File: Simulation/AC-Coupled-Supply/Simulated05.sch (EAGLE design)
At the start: 19 parts, among them IC1 78L05Z

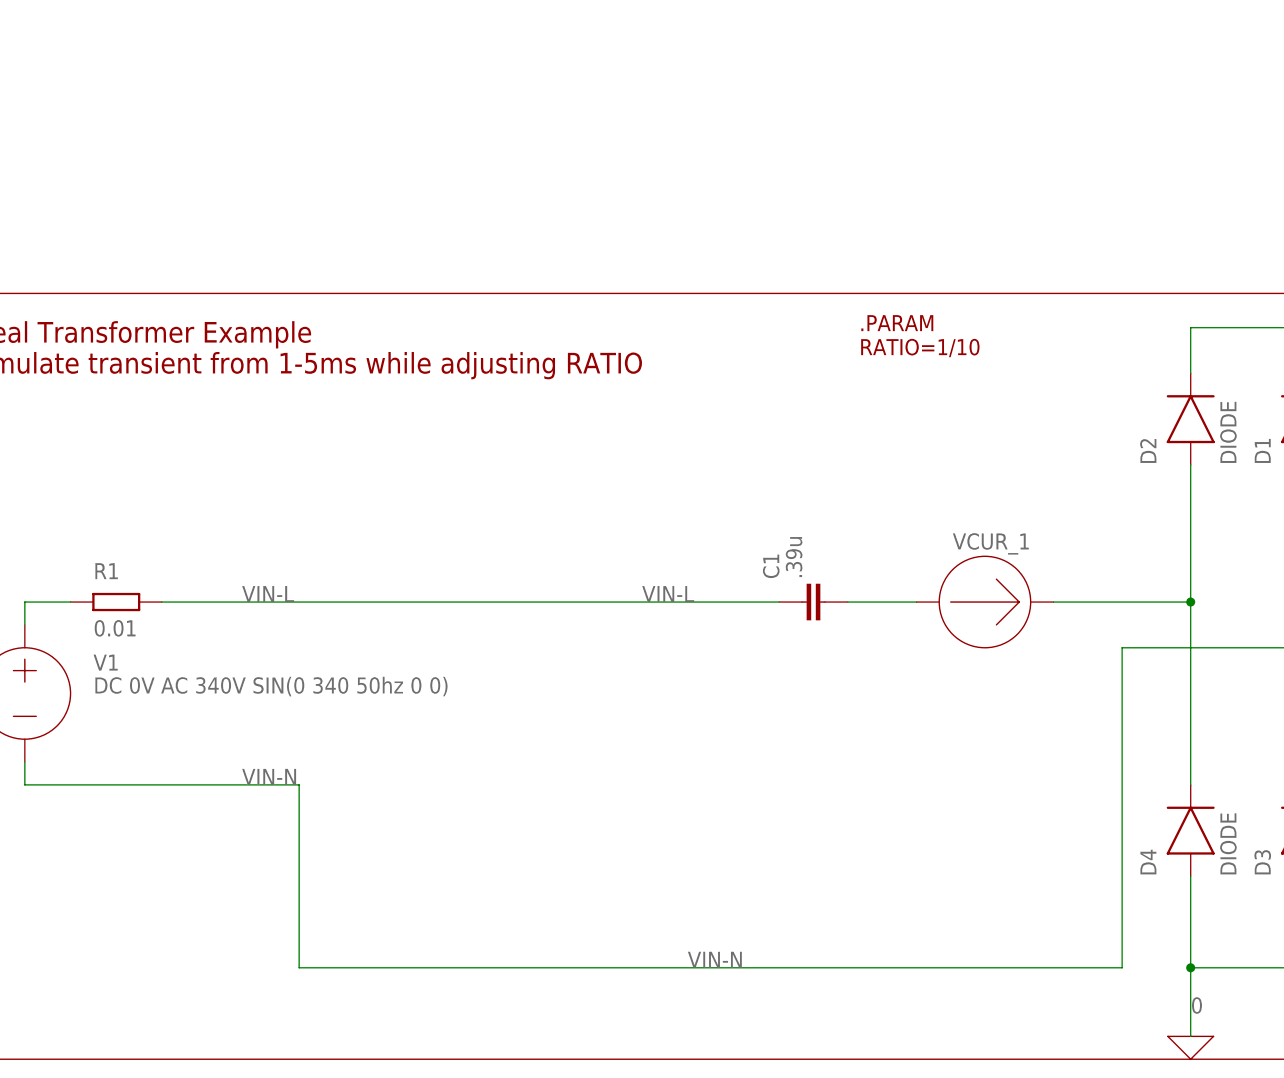
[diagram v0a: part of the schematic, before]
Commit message: measurement with differential probe
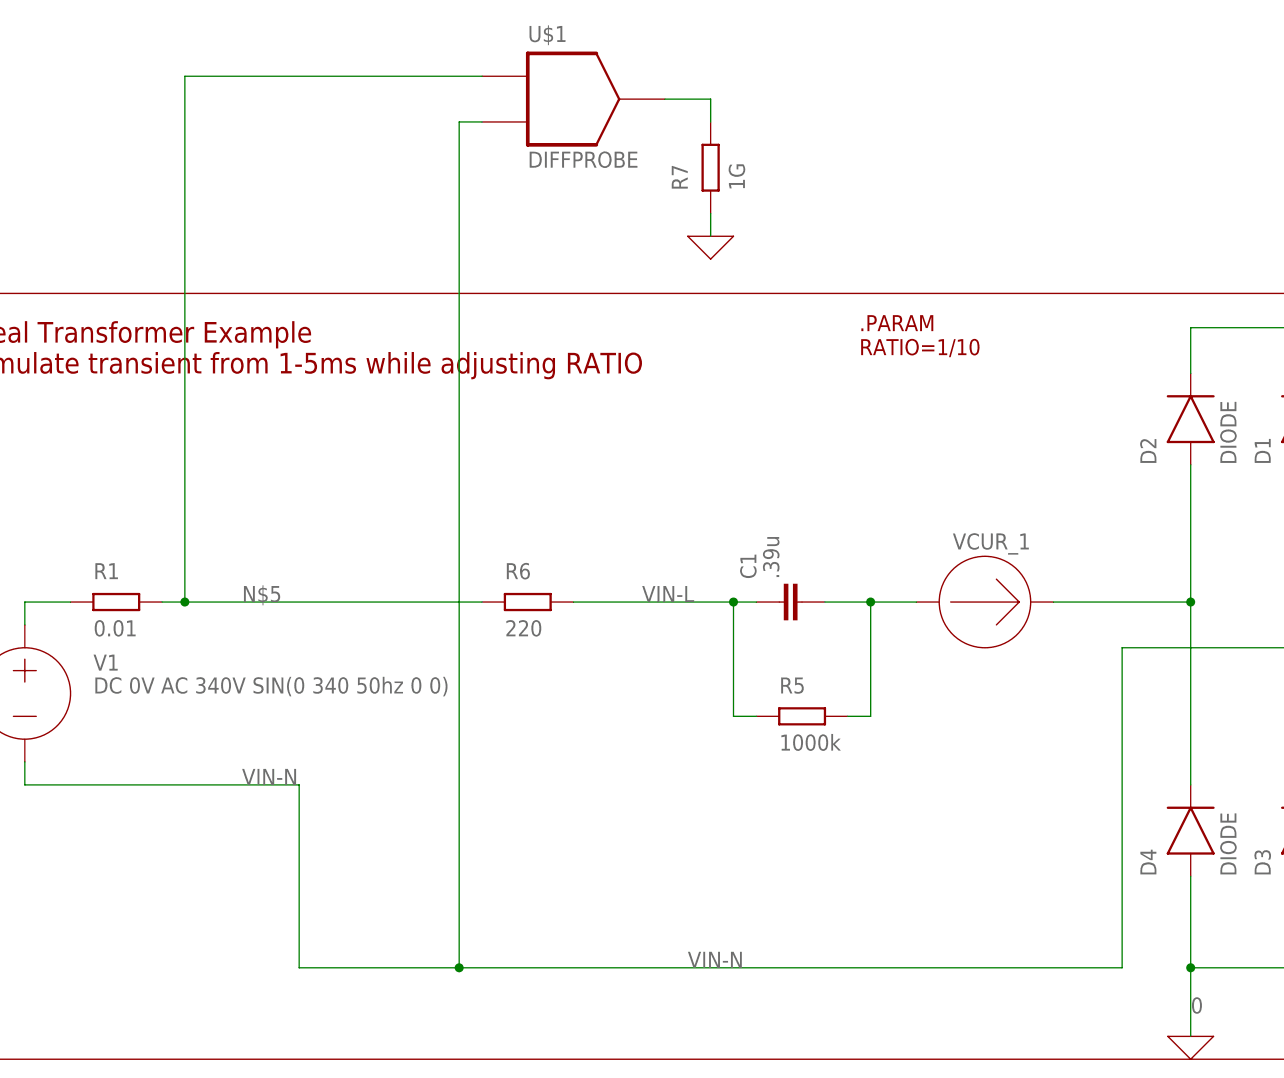
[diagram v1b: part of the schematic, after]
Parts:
- added R5: 1000k, ngspice-simulation:R
- added R6: 220, ngspice-simulation:R
- added R7: 1G, ngspice-simulation:R
- added U$1: DIFFPROBE, simulation:DIFFPROBE
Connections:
- new net DIFF: R7.2, U$1.OUT
- new net N$5: R1.2, R6.1, U$1.IN+
- net 0: now also R7.1
- net N$4: now also R5.2
- net VIN-L: now also R5.1, R6.2; no longer R1.2
- net VIN-N: now also U$1.IN-
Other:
- moved on the sheet: C1
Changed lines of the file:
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@@
 <layer number="48" name="Document" color="7" fill="1" visible="no" active="no"/>
 <layer number="49" name="Reference" color="7" fill="1" visible="no" active="no"/>
+<layer number="50" name="dxf" color="7" fill="1" visible="no" active="no"/>
 <layer number="51" name="tDocu" color="7" fill="1" visible="no" active="no"/>
 <layer number="52" name="bDocu" color="7" fill="1" visible="no" active="no"/>
@@
 <layer number="98" name="Guide" color="6" fill="1" visible="yes" active="yes"/>
 <layer number="99" name="SpiceOrder" color="7" fill="1" visible="yes" active="yes"/>
+<layer number="250" name="Descript" color="3" fill="1" visible="no" active="no"/>
+<layer number="251" name="SMDround" color="12" fill="11" visible="no" active="no"/>
 </layers>
 <schematic xreflabel="%F%N/%S.%C%R" xrefpart="/%S.%C%R">
@@
 <part name="C4" library="ngspice-simulation" library_urn="urn:adsk.eagle:library:527439" deviceset="C" device="" value="100n"/>
 <part name="R4" library="ngspice-simulation" library_urn="urn:adsk.eagle:library:5272020" deviceset="R" device="" value="1k"/>
+<part name="R5" library="ngspice-simulation" library_urn="urn:adsk.eagle:library:5272020" deviceset="R" device="" value="1000k"/>
+<part name="R6" library="ngspice-simulation" library_urn="urn:adsk.eagle:library:5272020" deviceset="R" device="" value="220"/>
+<part name="U$1" library="simulation" deviceset="DIFFPROBE" device=""/>
+<part name="R7" library="ngspice-simulation" library_urn="urn:adsk.eagle:library:5272020" deviceset="R" device="" value="1G"/>
+<part name="X_1" library="ngspice-simulation" library_urn="urn:adsk.eagle:library:5272020" deviceset="GND" device=""/>
 </parts>
 <sheets>
@@
 <attribute name="VALUE" x="176.53" y="55.88" size="1.778" layer="96" rot="R90"/>
 </instance>
-<instance part="C1" gate="G$1" x="96.52" y="38.1" smashed="yes" rot="R90">
-<attribute name="NAME" x="93.98" y="40.64" size="1.778" layer="95" rot="R90"/>
-<attribute name="VALUE" x="96.52" y="40.64" size="1.778" layer="96" rot="R90"/>
+<instance part="C1" gate="G$1" x="93.98" y="38.1" smashed="yes" rot="R90">
+<attribute name="NAME" x="91.44" y="40.64" size="1.778" layer="95" rot="R90"/>
+<attribute name="VALUE" x="93.98" y="40.64" size="1.778" layer="96" rot="R90"/>
 </instance>
 <instance part="D5" gate="G$1" x="172.72" y="12.7" smashed="yes" rot="R90">
@@
 <attribute name="VALUE" x="313.69" y="7.62" size="1.778" layer="96" rot="R90"/>
 </instance>
+<instance part="R5" gate="G$1" x="96.52" y="25.4" smashed="yes">
+<attribute name="NAME" x="93.98" y="27.94" size="1.778" layer="95"/>
+<attribute name="VALUE" x="93.98" y="21.59" size="1.778" layer="96"/>
+</instance>
+<instance part="R6" gate="G$1" x="66.04" y="38.1" smashed="yes">
+<attribute name="NAME" x="63.5" y="40.64" size="1.778" layer="95"/>
+<attribute name="VALUE" x="63.5" y="34.29" size="1.778" layer="96"/>
+</instance>
+<instance part="U$1" gate="G$1" x="71.12" y="93.98" smashed="yes">
+<attribute name="NAME" x="66.04" y="100.33" size="1.778" layer="95"/>
+<attribute name="VALUE" x="66.04" y="86.36" size="1.778" layer="96"/>
+</instance>
+<instance part="R7" gate="G$1" x="86.36" y="86.36" smashed="yes" rot="R90">
+<attribute name="NAME" x="83.82" y="83.82" size="1.778" layer="95" rot="R90"/>
+<attribute name="VALUE" x="90.17" y="83.82" size="1.778" layer="96" rot="R90"/>
+</instance>
+<instance part="X_1" gate="G$1" x="86.36" y="78.74" smashed="yes"/>
 </instances>
 <busses>
@@
 <net name="VIN-L" class="0">
 <segment>
-<pinref part="R1" gate="G$1" pin="2"/>
-<label x="34.29" y="38.1" size="1.778" layer="95"/>
 <label x="78.74" y="38.1" size="1.778" layer="95"/>
-<wire x1="25.4" y1="38.1" x2="93.98" y2="38.1" width="0.1524" layer="91"/>
 <pinref part="C1" gate="G$1" pin="1"/>
+<pinref part="R5" gate="G$1" pin="1"/>
+<wire x1="88.9" y1="38.1" x2="91.44" y2="38.1" width="0.1524" layer="91"/>
+<wire x1="91.44" y1="25.4" x2="88.9" y2="25.4" width="0.1524" layer="91"/>
+<wire x1="88.9" y1="25.4" x2="88.9" y2="38.1" width="0.1524" layer="91"/>
+<junction x="88.9" y="38.1"/>
+<wire x1="71.12" y1="38.1" x2="88.9" y2="38.1" width="0.1524" layer="91"/>
+<pinref part="R6" gate="G$1" pin="2"/>
 </segment>
 </net>
@@
 <label x="196.088" y="69.596" size="1.778" layer="95"/>
 <pinref part="R2" gate="G$1" pin="2"/>
-<wire x1="172.72" y1="63.5" x2="172.72" y2="68.58" width="0.1524" layer="91"/>
 <junction x="172.72" y="68.58"/>
 <probe x="170.18" y="71.12" size="1.778" layer="89" rot="R90" probetype="0"/>
+<wire x1="172.72" y1="63.5" x2="172.72" y2="68.58" width="0.1524" layer="91"/>
 </segment>
 </net>
@@
 <label x="34.29" y="17.78" size="1.778" layer="95"/>
 <wire x1="40.64" y1="17.78" x2="40.64" y2="-2.54" width="0.1524" layer="91"/>
-<wire x1="40.64" y1="-2.54" x2="132.08" y2="-2.54" width="0.1524" layer="91"/>
+<wire x1="40.64" y1="-2.54" x2="58.42" y2="-2.54" width="0.1524" layer="91"/>
 <label x="83.82" y="-2.54" size="1.778" layer="95"/>
 <pinref part="D1" gate="G$1" pin="A"/>
 <pinref part="D3" gate="G$1" pin="C"/>
+<wire x1="58.42" y1="-2.54" x2="132.08" y2="-2.54" width="0.1524" layer="91"/>
 <wire x1="152.4" y1="53.34" x2="152.4" y2="33.02" width="0.1524" layer="91"/>
 <wire x1="152.4" y1="33.02" x2="152.4" y2="17.78" width="0.1524" layer="91"/>
@@
 <wire x1="132.08" y1="33.02" x2="152.4" y2="33.02" width="0.1524" layer="91"/>
 <junction x="152.4" y="33.02"/>
+<pinref part="U$1" gate="G$1" pin="IN-"/>
+<wire x1="60.96" y1="91.44" x2="58.42" y2="91.44" width="0.1524" layer="91"/>
+<wire x1="58.42" y1="91.44" x2="58.42" y2="-2.54" width="0.1524" layer="91"/>
+<junction x="58.42" y="-2.54"/>
 </segment>
 </net>
@@
 <junction x="292.1" y="-2.54"/>
 </segment>
+<segment>
+<pinref part="R7" gate="G$1" pin="1"/>
+<pinref part="X_1" gate="G$1" pin="0"/>
+<wire x1="86.36" y1="81.28" x2="86.36" y2="78.74" width="0.1524" layer="91"/>
+</segment>
 </net>
 <net name="N$3" class="0">
@@
 <segment>
 <pinref part="C1" gate="G$1" pin="2"/>
-<wire x1="101.6" y1="38.1" x2="109.22" y2="38.1" width="0.1524" layer="91"/>
+<wire x1="99.06" y1="38.1" x2="104.14" y2="38.1" width="0.1524" layer="91"/>
 <pinref part="VCUR_1" gate="G$1" pin="+"/>
+<pinref part="R5" gate="G$1" pin="2"/>
+<wire x1="104.14" y1="38.1" x2="109.22" y2="38.1" width="0.1524" layer="91"/>
+<wire x1="101.6" y1="25.4" x2="104.14" y2="25.4" width="0.1524" layer="91"/>
+<wire x1="104.14" y1="25.4" x2="104.14" y2="38.1" width="0.1524" layer="91"/>
+<junction x="104.14" y="38.1"/>
 </segment>
 </net>
@@
 </segment>
 </net>
-<net name="N$1" class="0">
-<segment>
-<pinref part="R2" gate="G$1" pin="1"/>
-<wire x1="172.72" y1="48.26" x2="172.72" y2="53.34" width="0.1524" layer="91"/>
-<pinref part="VCUR_2" gate="G$1" pin="+"/>
-</segment>
-</net>
 <net name="VOUT" class="0">
 <segment>
@@
 </segment>
 </net>
+<net name="N$5" class="0">
+<segment>
+<pinref part="R1" gate="G$1" pin="2"/>
+<wire x1="25.4" y1="38.1" x2="27.94" y2="38.1" width="0.1524" layer="91"/>
+<label x="34.29" y="38.1" size="1.778" layer="95"/>
+<pinref part="R6" gate="G$1" pin="1"/>
+<probe x="48.26" y="48.26" size="1.778" layer="89" probetype="0"/>
+<pinref part="U$1" gate="G$1" pin="IN+"/>
+<wire x1="27.94" y1="38.1" x2="60.96" y2="38.1" width="0.1524" layer="91"/>
+<wire x1="60.96" y1="96.52" x2="27.94" y2="96.52" width="0.1524" layer="91"/>
+<wire x1="27.94" y1="96.52" x2="27.94" y2="38.1" width="0.1524" layer="91"/>
+<junction x="27.94" y="38.1"/>
+</segment>
+</net>
+<net name="DIFF" class="0">
+<segment>
+<pinref part="R7" gate="G$1" pin="2"/>
+<wire x1="86.36" y1="91.44" x2="86.36" y2="93.98" width="0.1524" layer="91"/>
+<pinref part="U$1" gate="G$1" pin="OUT"/>
+<wire x1="86.36" y1="93.98" x2="81.28" y2="93.98" width="0.1524" layer="91"/>
+<probe x="91.44" y="99.06" size="1.778" layer="89" probetype="0"/>
+</segment>
+</net>
+<net name="N$7" class="0">
+<segment>
+<pinref part="R2" gate="G$1" pin="1"/>
+<pinref part="VCUR_2" gate="G$1" pin="+"/>
+<wire x1="172.72" y1="48.26" x2="172.72" y2="53.34" width="0.1524" layer="91"/>
+</segment>
+</net>
